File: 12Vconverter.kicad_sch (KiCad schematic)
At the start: 6 parts, among them IC400 TLP185xSE

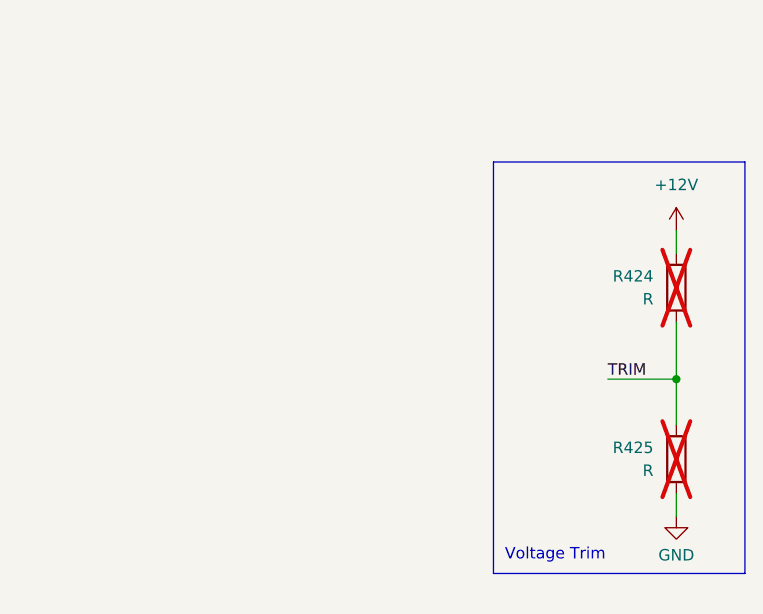
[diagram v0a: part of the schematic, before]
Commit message: Change MCU to STM32H563
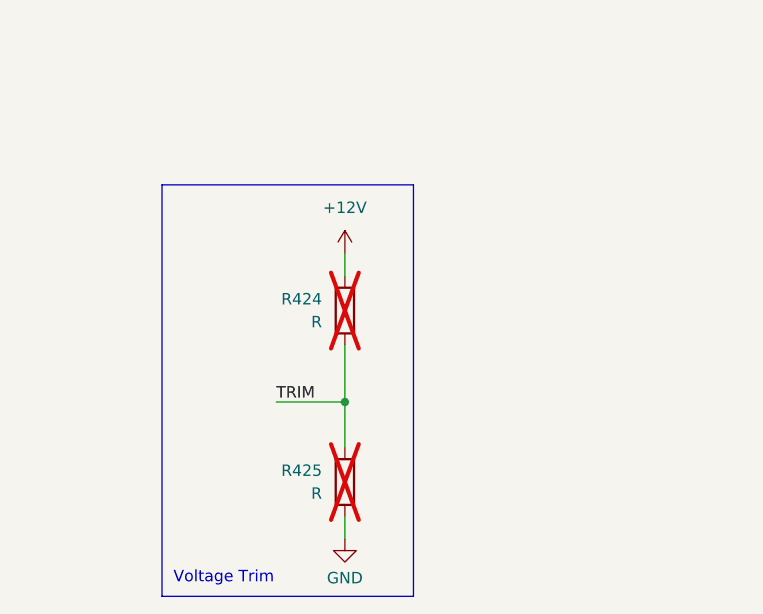
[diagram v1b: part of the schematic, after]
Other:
- moved on the sheet: R424, R425
